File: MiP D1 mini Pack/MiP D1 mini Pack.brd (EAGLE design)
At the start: 41.4 x 63.8 mm, 6 parts, among them J2 D1 mini, J3 Debug

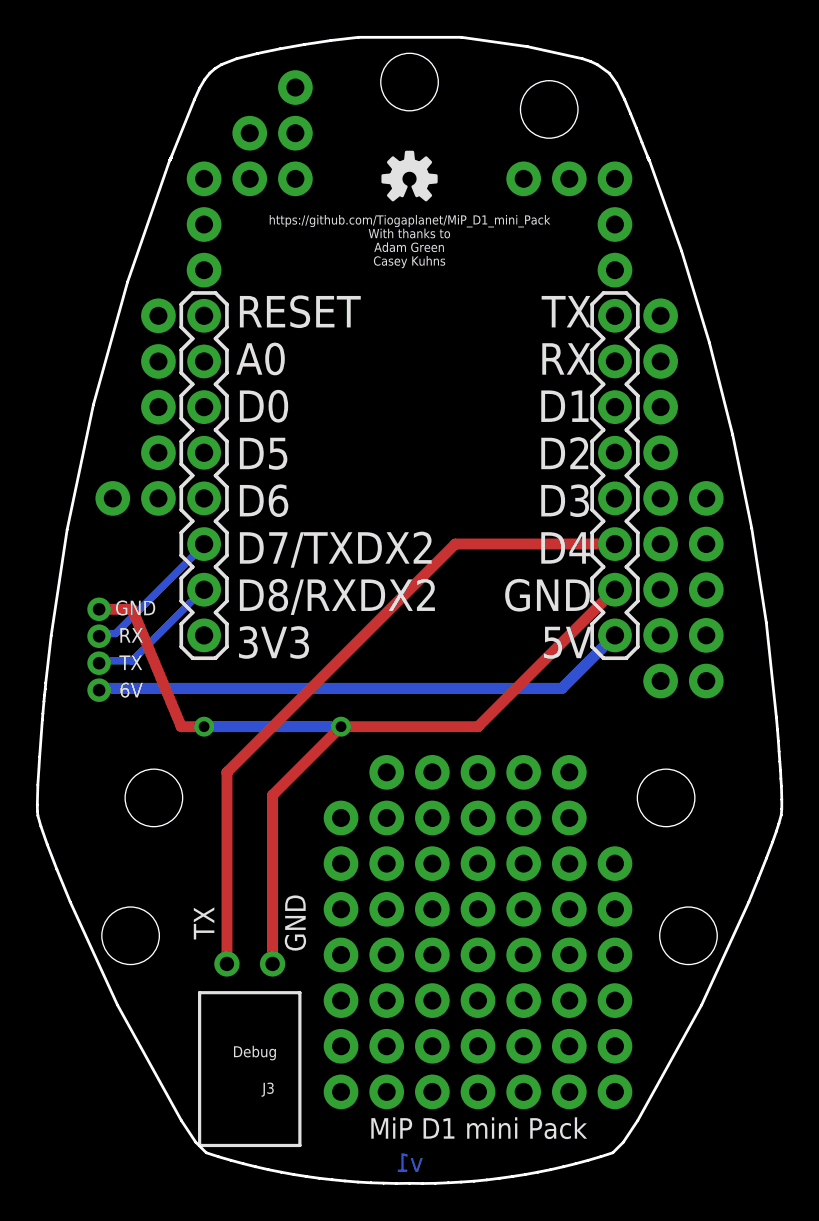
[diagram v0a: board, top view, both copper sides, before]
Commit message: Fixed rookie mistake (RX/TX was backwards)
Fixed twisted RX/TX pair, corrected labels, added labels for debug
connector, made minor moves.
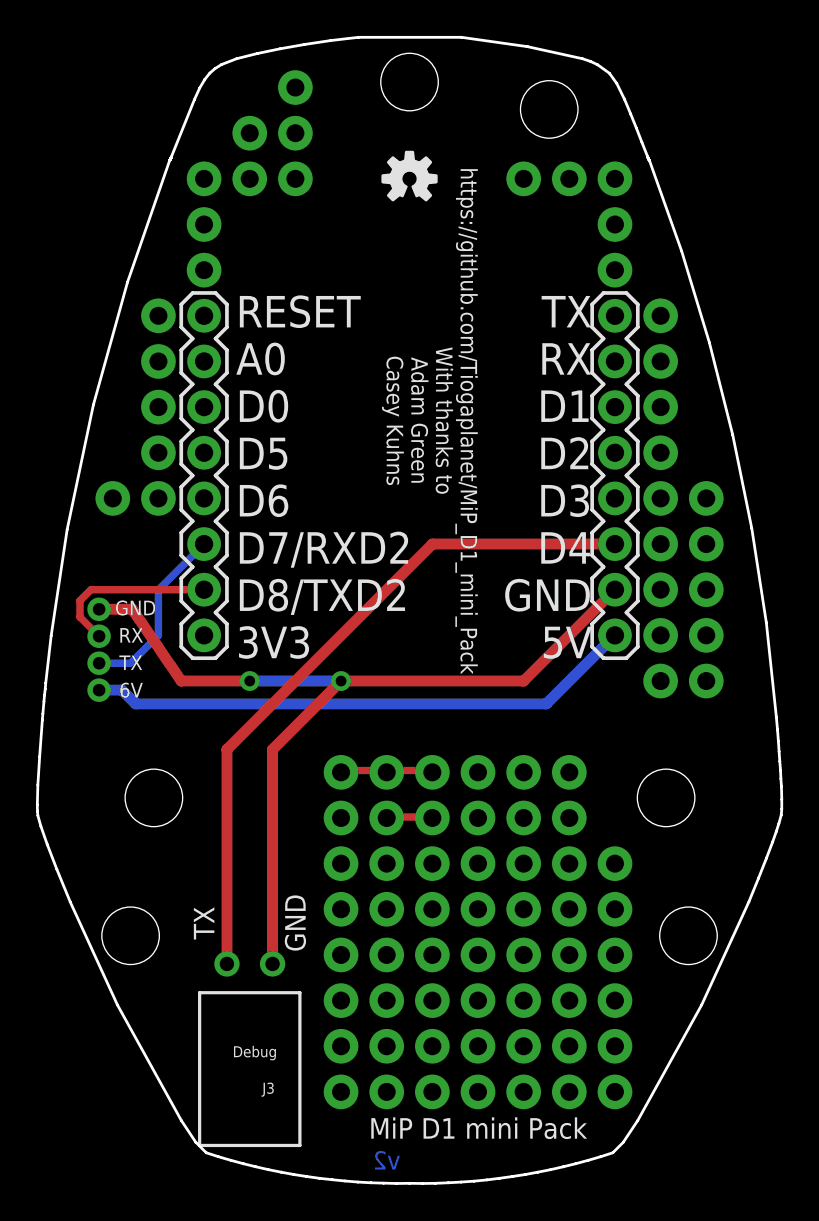
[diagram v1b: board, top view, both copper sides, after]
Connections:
- net N$4 renamed DEBUG
- net RX: now also JP11.3; no longer JP11.2
- net TX: now also JP11.2; no longer JP11.3
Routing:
- net N$30: track 0.00 -> 5.30 mm, vias 2 -> 3
- net N$96: track 0.00 -> 2.60 mm
- net RX: track 7.61 -> 9.67 mm
- net TX: track 8.07 -> 10.1 mm
- net GND: track 51.0 -> 50.2 mm
- net DEBUG: track 37.5 -> 38.3 mm
- net +6V: track 30.0 -> 30.6 mm
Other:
- board text added: "RESET A0 D0 D5 D6 D7/RXD2 D8/TXD2 3V3"
- board text added: "v2"
- board text removed: "RESET A0 D0 D5 D6 D7/TXDX2 D8/RXDX2 3V3"
- board text removed: "v1"

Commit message: Added net classes for RX and TX.
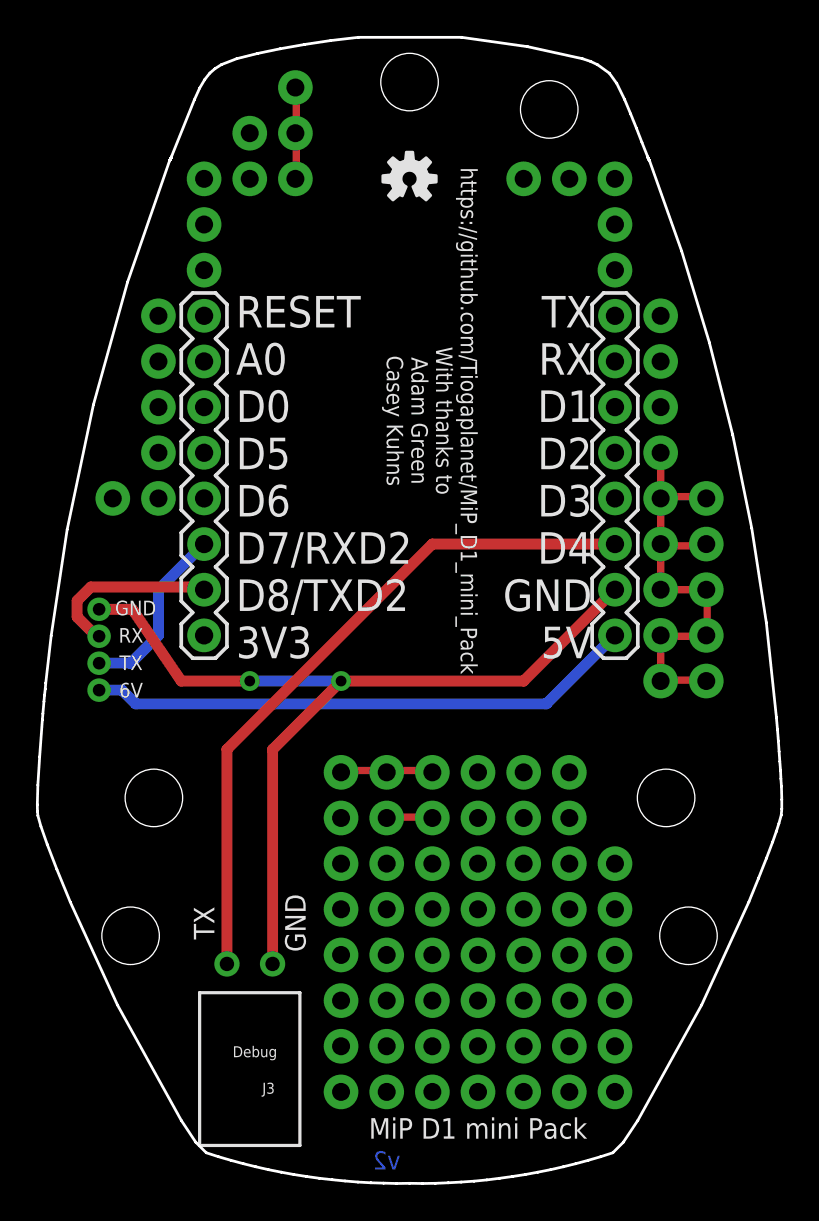
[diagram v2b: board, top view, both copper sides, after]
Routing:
- net N$53: track 0.00 -> 25.6 mm
- net N$1: track 0.00 -> 5.18 mm
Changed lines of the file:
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@@
 <class number="2" name="ground" width="0.6096" drill="0">
+</class>
+<class number="3" name="TX" width="0.6096" drill="0">
+</class>
+<class number="4" name="RX" width="0.6096" drill="0">
 </class>
 </classes>
@@
 <via x="38.1" y="29.21" extent="1-16" drill="1" diameter="1.9304"/>
 <via x="40.64" y="29.21" extent="1-16" drill="1" diameter="1.9304"/>
+<wire x1="38.1" y1="31.75" x2="38.1" y2="29.21" width="0.4064" layer="1"/>
+<wire x1="40.5384" y1="31.6992" x2="38.2524" y2="31.6992" width="0.4064" layer="1"/>
+<wire x1="38.2524" y1="31.6992" x2="38.1" y2="31.75" width="0.4064" layer="1"/>
+<wire x1="40.5384" y1="31.6992" x2="40.64" y2="31.75" width="0.4064" layer="1"/>
+<wire x1="38.2524" y1="29.2608" x2="40.5384" y2="29.2608" width="0.4064" layer="1"/>
+<wire x1="40.5384" y1="29.2608" x2="40.64" y2="29.21" width="0.4064" layer="1"/>
+<wire x1="38.2524" y1="29.2608" x2="38.1" y2="29.21" width="0.4064" layer="1"/>
+<wire x1="38.1" y1="36.83" x2="38.1" y2="34.29" width="0.4064" layer="1"/>
+<wire x1="40.5384" y1="36.7284" x2="38.2524" y2="36.7284" width="0.4064" layer="1"/>
+<wire x1="38.2524" y1="36.7284" x2="38.1" y2="36.83" width="0.4064" layer="1"/>
+<wire x1="40.5384" y1="36.7284" x2="40.64" y2="36.83" width="0.4064" layer="1"/>
+<wire x1="38.1" y1="34.29" x2="40.64" y2="34.29" width="0.4064" layer="1"/>
+<wire x1="38.1" y1="36.83" x2="38.1" y2="39.37" width="0.4064" layer="1"/>
+<wire x1="38.2524" y1="39.4716" x2="40.5384" y2="39.4716" width="0.4064" layer="1"/>
+<wire x1="40.5384" y1="39.4716" x2="40.64" y2="39.37" width="0.4064" layer="1"/>
+<wire x1="38.2524" y1="39.4716" x2="38.1" y2="39.37" width="0.4064" layer="1"/>
+<wire x1="38.1" y1="39.37" x2="38.1" y2="41.91" width="0.4064" layer="1"/>
+<wire x1="40.6908" y1="34.1376" x2="40.6908" y2="31.8516" width="0.4064" layer="1"/>
+<wire x1="40.6908" y1="31.8516" x2="40.64" y2="31.75" width="0.4064" layer="1"/>
+<wire x1="40.6908" y1="34.1376" x2="40.64" y2="34.29" width="0.4064" layer="1"/>
 </signal>
 <signal name="N$55">
@@
 <via x="17.78" y="59.69" extent="1-16" drill="1" diameter="1.9304"/>
 <via x="17.78" y="62.23" extent="1-16" drill="1" diameter="1.9304"/>
+<wire x1="17.8308" y1="59.5884" x2="17.8308" y2="57.15" width="0.4064" layer="1"/>
+<wire x1="17.8308" y1="57.15" x2="17.78" y2="57.15" width="0.4064" layer="1"/>
+<wire x1="17.8308" y1="59.5884" x2="17.78" y2="59.69" width="0.4064" layer="1"/>
+<wire x1="17.8308" y1="62.1792" x2="17.8308" y2="59.7408" width="0.4064" layer="1"/>
+<wire x1="17.8308" y1="59.7408" x2="17.78" y2="59.69" width="0.4064" layer="1"/>
+<wire x1="17.8308" y1="62.1792" x2="17.78" y2="62.23" width="0.4064" layer="1"/>
 </signal>
 <signal name="N$4">
@@
 <via x="20.32" y="11.43" extent="1-16" drill="1" diameter="1.9304"/>
 </signal>
-<signal name="RX">
+<signal name="RX" class="4">
 <contactref element="JP11" pad="3"/>
 <contactref element="J1" pad="2"/>
-<wire x1="6.7056" y1="31.8516" x2="6.858" y2="31.8516" width="0.4064" layer="1"/>
-<wire x1="5.7912" y1="32.766" x2="6.7056" y2="31.8516" width="0.4064" layer="1"/>
-<wire x1="5.7912" y1="33.6804" x2="5.7912" y2="32.766" width="0.4064" layer="1"/>
-<wire x1="6.4008" y1="34.29" x2="5.7912" y2="33.6804" width="0.4064" layer="1"/>
-<wire x1="12.7" y1="34.29" x2="6.4008" y2="34.29" width="0.4064" layer="1"/>
-<wire x1="6.858" y1="31.8516" x2="6.858" y2="31.702" width="0.4064" layer="1"/>
-</signal>
-<signal name="TX">
+<wire x1="6.5532" y1="31.8516" x2="6.858" y2="31.8516" width="0.6096" layer="1"/>
+<wire x1="5.6388" y1="32.766" x2="6.5532" y2="31.8516" width="0.6096" layer="1"/>
+<wire x1="5.6388" y1="33.6804" x2="5.6388" y2="32.766" width="0.6096" layer="1"/>
+<wire x1="6.4008" y1="34.4424" x2="5.6388" y2="33.6804" width="0.6096" layer="1"/>
+<wire x1="12.4968" y1="34.4424" x2="6.4008" y2="34.4424" width="0.6096" layer="1"/>
+<wire x1="12.6492" y1="34.29" x2="12.4968" y2="34.4424" width="0.6096" layer="1"/>
+<wire x1="6.858" y1="31.8516" x2="6.858" y2="31.702" width="0.6096" layer="1"/>
+<wire x1="12.6492" y1="34.29" x2="12.7" y2="34.29" width="0.6096" layer="1"/>
+</signal>
+<signal name="TX" class="3">
 <contactref element="JP11" pad="2"/>
 <contactref element="J1" pad="3"/>
-<wire x1="6.858" y1="30.202" x2="8.612" y2="30.202" width="0.4064" layer="16"/>
-<wire x1="8.612" y1="30.202" x2="10.16" y2="31.75" width="0.4064" layer="16"/>
-<wire x1="10.16" y1="31.75" x2="10.16" y2="34.29" width="0.4064" layer="16"/>
-<wire x1="10.16" y1="34.29" x2="12.7" y2="36.83" width="0.4064" layer="16"/>
+<wire x1="6.858" y1="30.202" x2="8.612" y2="30.202" width="0.6096" layer="16"/>
+<wire x1="8.612" y1="30.202" x2="10.16" y2="31.75" width="0.6096" layer="16"/>
+<wire x1="10.16" y1="31.75" x2="10.16" y2="34.29" width="0.6096" layer="16"/>
+<wire x1="10.16" y1="34.29" x2="12.7" y2="36.83" width="0.6096" layer="16"/>
 </signal>
 <signal name="+6V">

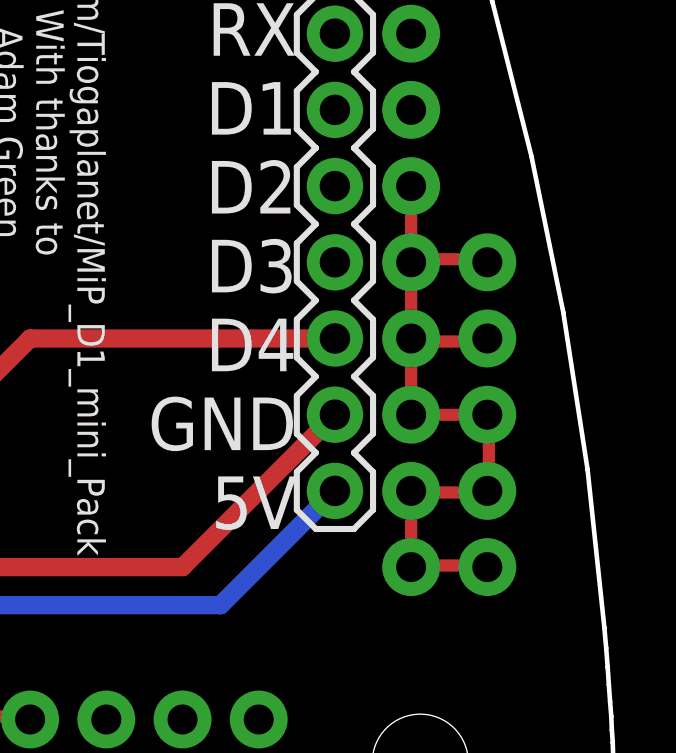
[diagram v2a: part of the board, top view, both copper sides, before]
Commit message: Fixed breadboard holes
Several breadboad holes had been accidentally connected.
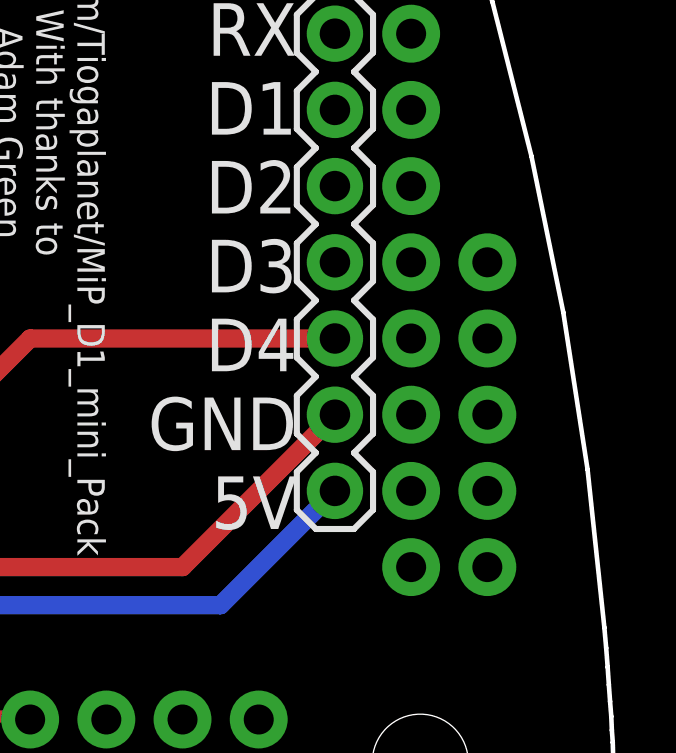
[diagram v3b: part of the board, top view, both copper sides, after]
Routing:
- net N$53: track 25.6 -> 0.00 mm, vias 11 -> 1
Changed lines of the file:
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@@
 <via x="38.1" y="44.45" extent="1-16" drill="1" diameter="1.9304"/>
+</signal>
+<signal name="N$18">
+<via x="40.64" y="29.21" extent="1-16" drill="1" diameter="1.9304"/>
+</signal>
+<signal name="N$19">
+<via x="38.1" y="29.21" extent="1-16" drill="1" diameter="1.9304"/>
+</signal>
+<signal name="N$22">
+<via x="38.1" y="31.75" extent="1-16" drill="1" diameter="1.9304"/>
+<via x="40.64" y="31.75" extent="1-16" drill="1" diameter="1.9304"/>
+</signal>
+<signal name="N$26">
+<via x="38.1" y="34.29" extent="1-16" drill="1" diameter="1.9304"/>
+</signal>
+<signal name="N$28">
+<via x="40.64" y="36.83" extent="1-16" drill="1" diameter="1.9304"/>
+<via x="40.64" y="34.29" extent="1-16" drill="1" diameter="1.9304"/>
+</signal>
+<signal name="N$31">
+<via x="38.1" y="36.83" extent="1-16" drill="1" diameter="1.9304"/>
+</signal>
+<signal name="N$33">
+<via x="40.64" y="39.37" extent="1-16" drill="1" diameter="1.9304"/>
+</signal>
+<signal name="N$36">
+<via x="38.1" y="39.37" extent="1-16" drill="1" diameter="1.9304"/>
 </signal>
 <signal name="N$53">
 <via x="38.1" y="41.91" extent="1-16" drill="1" diameter="1.9304"/>
-<via x="38.1" y="39.37" extent="1-16" drill="1" diameter="1.9304"/>
-<via x="38.1" y="36.83" extent="1-16" drill="1" diameter="1.9304"/>
-<via x="38.1" y="34.29" extent="1-16" drill="1" diameter="1.9304"/>
-<via x="38.1" y="31.75" extent="1-16" drill="1" diameter="1.9304"/>
-<via x="40.64" y="31.75" extent="1-16" drill="1" diameter="1.9304"/>
-<via x="40.64" y="34.29" extent="1-16" drill="1" diameter="1.9304"/>
-<via x="40.64" y="36.83" extent="1-16" drill="1" diameter="1.9304"/>
-<via x="40.64" y="39.37" extent="1-16" drill="1" diameter="1.9304"/>
-<via x="38.1" y="29.21" extent="1-16" drill="1" diameter="1.9304"/>
-<via x="40.64" y="29.21" extent="1-16" drill="1" diameter="1.9304"/>
-<wire x1="38.1" y1="31.75" x2="38.1" y2="29.21" width="0.4064" layer="1"/>
-<wire x1="40.5384" y1="31.6992" x2="38.2524" y2="31.6992" width="0.4064" layer="1"/>
-<wire x1="38.2524" y1="31.6992" x2="38.1" y2="31.75" width="0.4064" layer="1"/>
-<wire x1="40.5384" y1="31.6992" x2="40.64" y2="31.75" width="0.4064" layer="1"/>
-<wire x1="38.2524" y1="29.2608" x2="40.5384" y2="29.2608" width="0.4064" layer="1"/>
-<wire x1="40.5384" y1="29.2608" x2="40.64" y2="29.21" width="0.4064" layer="1"/>
-<wire x1="38.2524" y1="29.2608" x2="38.1" y2="29.21" width="0.4064" layer="1"/>
-<wire x1="38.1" y1="36.83" x2="38.1" y2="34.29" width="0.4064" layer="1"/>
-<wire x1="40.5384" y1="36.7284" x2="38.2524" y2="36.7284" width="0.4064" layer="1"/>
-<wire x1="38.2524" y1="36.7284" x2="38.1" y2="36.83" width="0.4064" layer="1"/>
-<wire x1="40.5384" y1="36.7284" x2="40.64" y2="36.83" width="0.4064" layer="1"/>
-<wire x1="38.1" y1="34.29" x2="40.64" y2="34.29" width="0.4064" layer="1"/>
-<wire x1="38.1" y1="36.83" x2="38.1" y2="39.37" width="0.4064" layer="1"/>
-<wire x1="38.2524" y1="39.4716" x2="40.5384" y2="39.4716" width="0.4064" layer="1"/>
-<wire x1="40.5384" y1="39.4716" x2="40.64" y2="39.37" width="0.4064" layer="1"/>
-<wire x1="38.2524" y1="39.4716" x2="38.1" y2="39.37" width="0.4064" layer="1"/>
-<wire x1="38.1" y1="39.37" x2="38.1" y2="41.91" width="0.4064" layer="1"/>
-<wire x1="40.6908" y1="34.1376" x2="40.6908" y2="31.8516" width="0.4064" layer="1"/>
-<wire x1="40.6908" y1="31.8516" x2="40.64" y2="31.75" width="0.4064" layer="1"/>
-<wire x1="40.6908" y1="34.1376" x2="40.64" y2="34.29" width="0.4064" layer="1"/>
 </signal>
 <signal name="N$55">
